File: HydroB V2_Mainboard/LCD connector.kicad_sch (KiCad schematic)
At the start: 24 parts, among them J1 Conn_01x52_Pin, J2 Conn_01x08_Pin

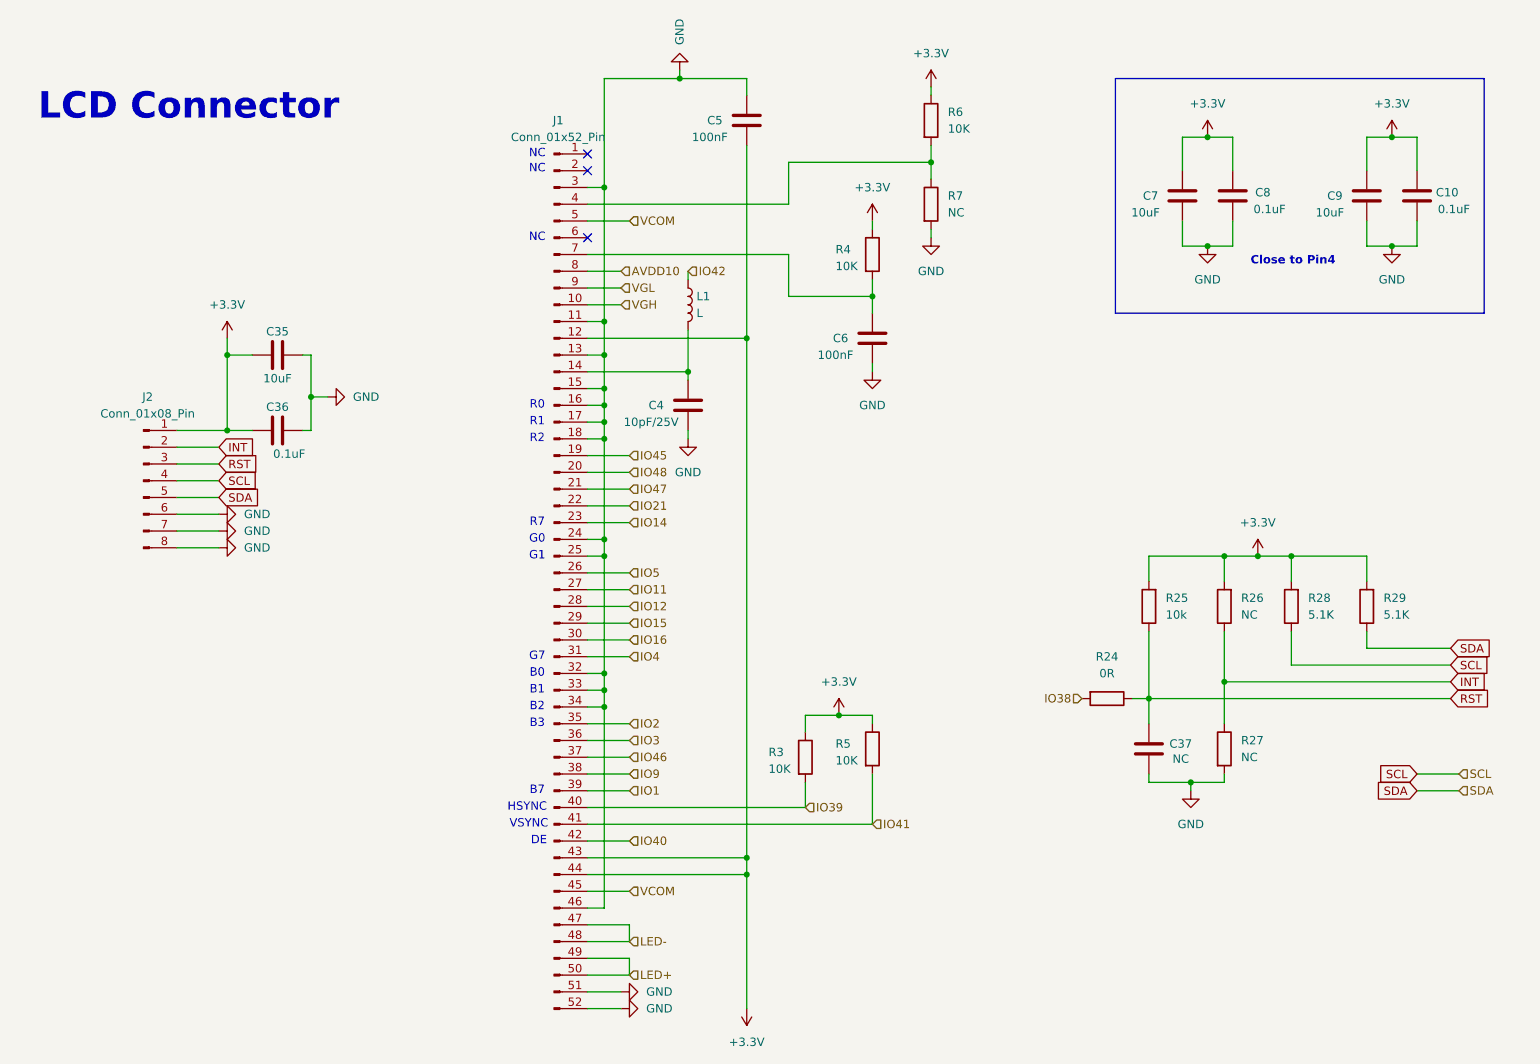
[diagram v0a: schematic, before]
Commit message: Update LCD schematic
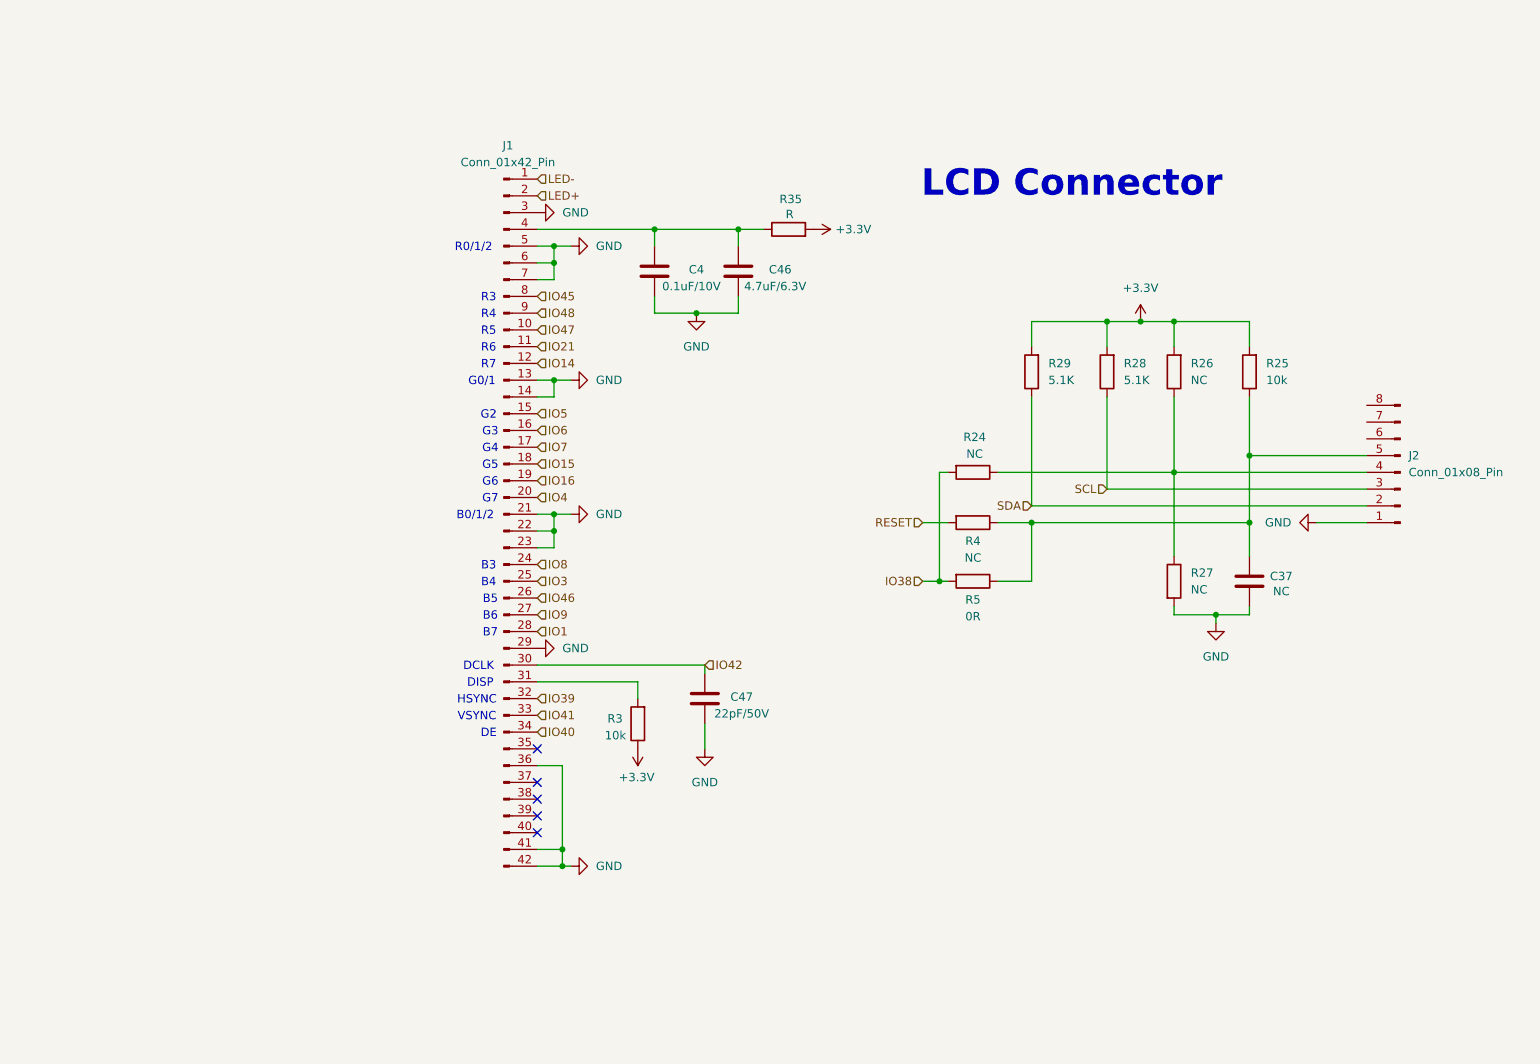
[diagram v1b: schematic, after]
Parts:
- removed C10, C36, C8: 0.1uF, Capacitor_SMD:C_0603_1608Metric, symbol Device:C
- removed C35, C7, C9: 10uF, Capacitor_SMD:C_0603_1608Metric, symbol Device:C
- removed C5, C6: 100nF, Capacitor_SMD:C_0603_1608Metric, symbol Device:C
- removed J1: Conn_01x52_Pin, symbol Connector:Conn_01x52_Pin
- removed L1: L, Inductor_SMD:L_Bourns_SRR1260, symbol Device:L
- removed R6: 10K, Resistor_SMD:R_0603_1608Metric, symbol Device:R
- removed R7: NC, Resistor_SMD:R_0603_1608Metric, symbol Device:R
- added C46: 4.7uF/6.3V, Capacitor_SMD:C_0805_2012Metric, symbol Device:C
- added C47: 22pF/50V, Capacitor_SMD:C_0805_2012Metric, symbol Device:C
- added J1: Conn_01x42_Pin, symbol Connector:Conn_01x42_Pin
- added R35: R, Resistor_SMD:R_0603_1608Metric, symbol Device:R
- C4: value 10pF/25V -> 0.1uF/10V
- R24: value 0R -> NC
- R3: value 10K -> 10k
- R4: value 10K -> NC; footprint Resistor_SMD:R_0603_1608Metric -> Resistor_SMD:R_0402_1005Metric; LCSC (none) -> C25744; MFR (none) -> 0402WGF1002TCE
- R5: value 10K -> 0R; footprint Resistor_SMD:R_0603_1608Metric -> Resistor_SMD:R_0402_1005Metric; LCSC (none) -> C25744; MFR (none) -> 0402WGF1002TCE
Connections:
- net +3.3V: now also R35.2; no longer J2.1 (Pin_1), R4.1, R5.1
- net GND: now also J2.1 (Pin_1), C46.1, C47.1, J1.13 (Pin_13), J1.14 (Pin_14), J1.21 (Pin_21), J1.22 (Pin_22), J1.23 (Pin_23), J1.29 (Pin_29), J1.3 (Pin_3), J1.36 (Pin_36), J1.41 (Pin_41), J1.42 (Pin_42), J1.5 (Pin_5), J1.6 (Pin_6), J1.7 (Pin_7); no longer J2.6 (Pin_6), J2.7 (Pin_7), J2.8 (Pin_8)
- net IO1: now also J1.28 (Pin_28)
- net IO14: now also J1.12 (Pin_12)
- net IO15: now also J1.18 (Pin_18)
- net IO16: now also J1.19 (Pin_19)
- net IO21: now also J1.11 (Pin_11)
- net IO3: now also J1.25 (Pin_25)
- net IO38: now also R5.2
- net IO39: now also J1.32 (Pin_32); no longer R3.2
- net IO4: now also J1.20 (Pin_20)
- net IO40: now also J1.34 (Pin_34)
- net IO41: now also J1.33 (Pin_33); no longer R5.2
- net IO42: now also C47.2, J1.30 (Pin_30)
- net IO45: now also J1.8 (Pin_8)
- net IO46: now also J1.26 (Pin_26)
- net IO47: now also J1.10 (Pin_10)
- net IO48: now also J1.9 (Pin_9)
- net IO5: now also J1.15 (Pin_15)
- net IO9: now also J1.27 (Pin_27)
- net LED+: now also J1.2 (Pin_2)
- net LED-: now also J1.1 (Pin_1)
- net SCL: now also J2.3 (Pin_3); no longer J2.4 (Pin_4)
- net SDA: now also J2.2 (Pin_2); no longer J2.5 (Pin_5)
- net RESET: now reaches R4.2
- net at C4.2: now also C46.2, J1.4 (Pin_4), R35.1
- net INT: no longer names the net of R26.1, R27.1
- net INT: now also J2.4 (Pin_4), R24.1; no longer J2.2 (Pin_2)
- net RST: no longer names the net of C37.2, R25.1
- net RST: now also J2.5 (Pin_5), R4.1, R5.1; no longer J2.3 (Pin_3), R24.1
- new net: J1.31 (Pin_31), R3.2
- new net IO6: J1.16 (Pin_16)
- new net IO7: J1.17 (Pin_17)
- new net IO8: J1.24 (Pin_24)
- no-connect marks 3 -> 5
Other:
- note added: "B0/1/2"
- note added: "B4"
- note added: "B5"
- note added: "B6"
- note added: "DCLK"
- note added: "DISP"
- note added: "G0/1"
- note added: "G2"
- note added: "G3"
- note added: "G4"
- note added: "G5"
- note added: "G6"
- note added: "R0/1/2"
- note added: "R3"
- note added: "R4"
- note added: "R5"
- note added: "R6"
- note removed: "B0"
- note removed: "B1"
- note removed: "B2"
- note removed: "Close to Pin4"
- note removed: "G0"
- note removed: "G1"
- note removed: "NC"
- note removed: "R0"
- note removed: "R1"
- note removed: "R2"
- moved on the sheet: C37, C4, J2, R24, R25, R26, R27, R28, R29

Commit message: Schematic mainboard update
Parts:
- removed C37: NC, Capacitor_SMD:C_0603_1608Metric, symbol Device:C
- removed J1: Conn_01x42_Pin, symbol Connector:Conn_01x42_Pin
- removed R24, R27: NC, Resistor_SMD:R_0402_1005Metric, symbol Device:R
- removed R5: 0R, Resistor_SMD:R_0402_1005Metric, symbol Device:R
- added C6: 100nF, Capacitor_SMD:C_0603_1608Metric, symbol Device:C
- added J6: Conn_01x40_Pin, symbol Connector:Conn_01x40_Pin
- C46, C47: footprint Capacitor_SMD:C_0805_2012Metric -> Capacitor_SMD:C_0603_1608Metric
- J2: footprint (none) -> Connector_FFC-FPC:Hirose_FH12-6S-0.5SH_1x06-1MP_P0.50mm_Horizontal
- R25: footprint Resistor_SMD:R_0402_1005Metric -> Resistor_SMD:R_0603_1608Metric
- R26: value NC -> 10k; footprint Resistor_SMD:R_0402_1005Metric -> Resistor_SMD:R_0603_1608Metric
- R28, R29: value 5.1K -> 10k; footprint Resistor_SMD:R_0402_1005Metric -> Resistor_SMD:R_0603_1608Metric
- R4: value NC -> 10k; footprint Resistor_SMD:R_0402_1005Metric -> Resistor_SMD:R_0603_1608Metric; LCSC C25744 -> (none); MFR 0402WGF1002TCE -> (none)
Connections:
- net +3.3V: now also J2.2 (Pin_2), R4.1, C6.2
- net GND: now also J2.3 (Pin_3), J2.7 (Pin_7), J2.8 (Pin_8), C6.1, J6.29 (Pin_29), J6.3 (Pin_3), J6.36 (Pin_36); no longer J2.1 (Pin_1)
- net LED+: now also J6.2 (Pin_2)
- net LED-: now also J6.1 (Pin_1)
- net SCL: now also J2.6 (Pin_6), R25.1; no longer J2.3 (Pin_3), R28.1
- net SDA: now also J2.5 (Pin_5), R26.1; no longer J2.2 (Pin_2), R29.1
- net at C4.2, C46.2, R35.1: now also J6.4 (Pin_4)
- net at R3.2: now also J6.31 (Pin_31)
- net INT: now reaches J2.4 (Pin_4)
- net INT: now also R28.1; no longer R26.1
- net IO42 renamed LCD_PCLK
- net LCD_PCLK: now also J6.30 (Pin_30)
- net RESET: no longer names the net of R4.2
- net RESET: now also J6.35 (Pin_35)
- new net B0: J6.5 (Pin_5)
- new net B1: J6.6 (Pin_6)
- new net B2: J6.7 (Pin_7)
- new net B3: J6.8 (Pin_8)
- new net B4: J6.9 (Pin_9)
- new net B5: J6.10 (Pin_10)
- new net B6: J6.11 (Pin_11)
- new net B7: J6.12 (Pin_12)
- new net G0: J6.13 (Pin_13)
- new net G1: J6.14 (Pin_14)
- new net G2: J6.15 (Pin_15)
- new net G3: J6.16 (Pin_16)
- new net G4: J6.17 (Pin_17)
- new net G5: J6.18 (Pin_18)
- new net G6: J6.19 (Pin_19)
- new net G7: J6.20 (Pin_20)
- new net HSYNC: J6.32 (Pin_32)
- new net LCD_DE: J6.34 (Pin_34)
- new net R0: J6.21 (Pin_21)
- new net R1: J6.22 (Pin_22)
- new net R2: J6.23 (Pin_23)
- new net R3: J6.24 (Pin_24)
- new net R4: J6.25 (Pin_25)
- new net R5: J6.26 (Pin_26)
- new net R6: J6.27 (Pin_27)
- new net R7: J6.28 (Pin_28)
- new net RST: J2.1 (Pin_1), R29.1
- new net VSYNC: J6.33 (Pin_33)
- new net X+: J6.37 (Pin_37)
- new net X-: J6.39 (Pin_39)
- new net Y+: J6.38 (Pin_38)
- new net Y-: J6.40 (Pin_40)
- no-connect marks 5 -> 0
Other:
- note removed: "B0/1/2"
- note removed: "B3"
- note removed: "B4"
- note removed: "B5"
- note removed: "B6"
- note removed: "B7"
- note removed: "G0/1"
- note removed: "G2"
- note removed: "G3"
- note removed: "G4"
- note removed: "G5"
- note removed: "G6"
- note removed: "G7"
- note removed: "R0/1/2"
- note removed: "R3"
- note removed: "R4"
- note removed: "R5"
- note removed: "R6"
- note removed: "R7"
- moved on the sheet: J2, R3

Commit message: Mainboard schematic update
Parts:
- removed R25, R26, R28, R29: 10k, Resistor_SMD:R_0603_1608Metric, symbol Device:R
- added RN1: CAY16-1002F4LF, CAY16-1002F4LF:RESCAF80P320X160X60-8N, symbol CAY16-1002F4LF:CAY16-1002F4LF
- C4: value 0.1uF/10V -> 0.1uF; footprint Capacitor_SMD:C_0805_2012Metric -> Capacitor_SMD:C_0603_1608Metric
- C46: value 4.7uF/6.3V -> 4.7uF
- C47: value 22pF/50V -> 22pF
- J6: footprint (none) -> Connector_FFC-FPC:TE_4-1734839-0_1x40-1MP_P0.5mm_Horizontal
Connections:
- net +3.3V: now also RN1.5, RN1.6, RN1.7, RN1.8
- net INT: now also RN1.2
- net RST: now also RN1.1
- net SCL: now also RN1.4
- net SDA: now also RN1.3
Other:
- moved on the sheet: C6, J2
